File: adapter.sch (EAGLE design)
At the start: 10 parts

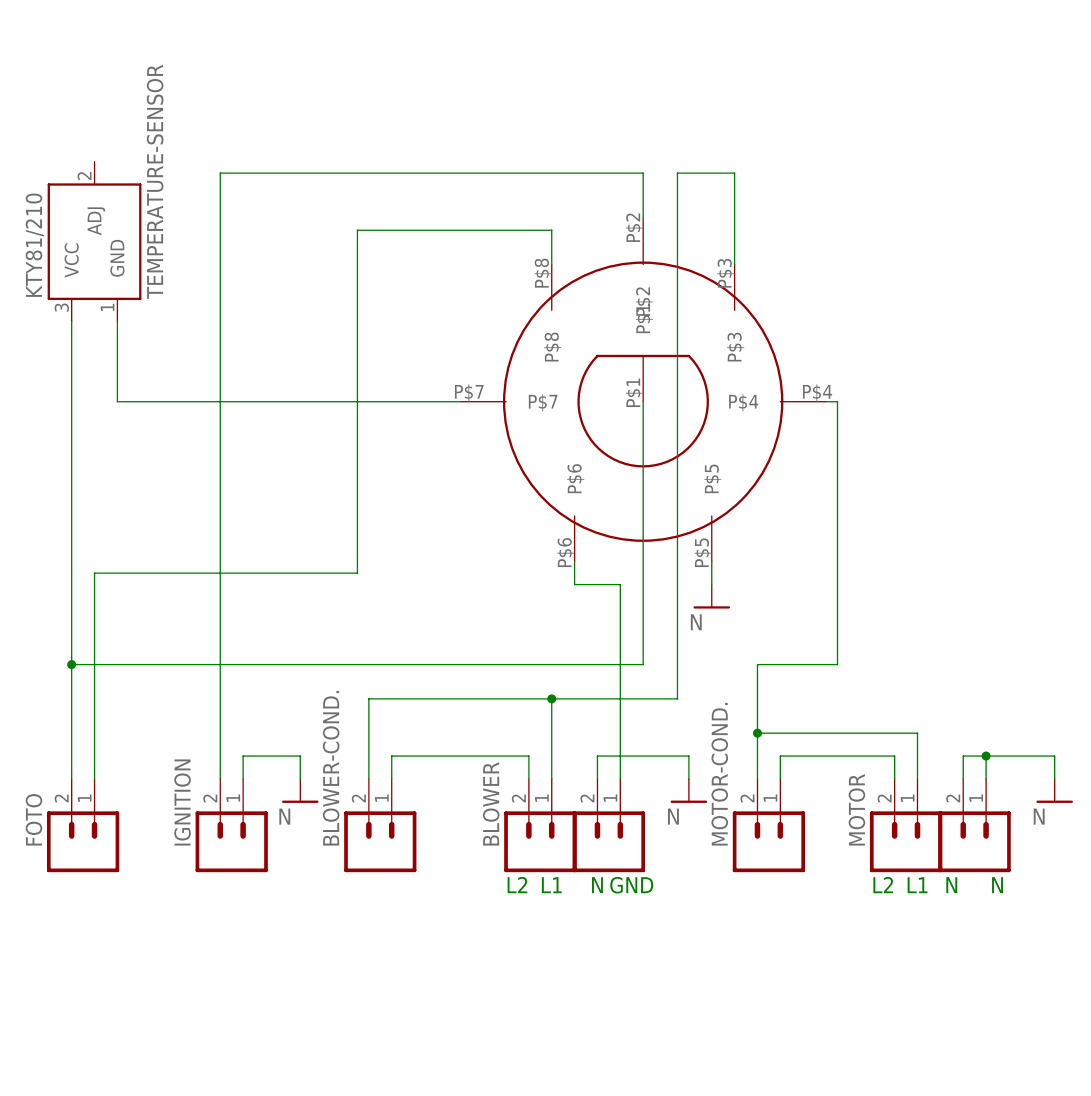
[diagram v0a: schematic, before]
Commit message: new version (v.1.4)
socket pin spacing changed from 5,02 mm to 5 mm

grouped photo and ignition connectors

added more silk info

wider pcb with space for capacitor hole mount
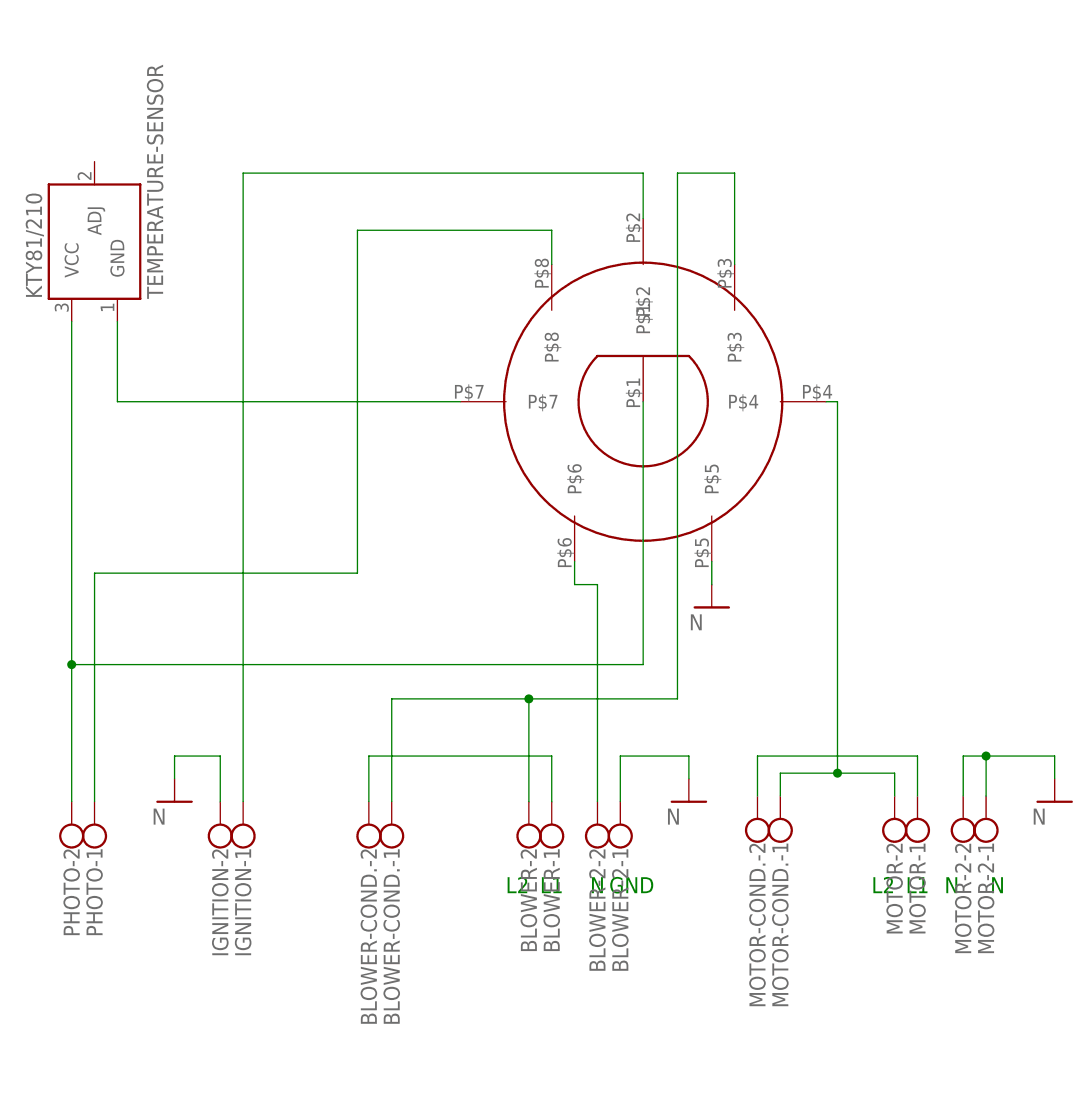
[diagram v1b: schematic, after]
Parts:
- removed BLOWER1, FOTO, MOTOR1: (no value), SparkFun (old):M02PTH3_5MM
- added BLOWER-2, MOTOR-2, PHOTO: (no value), con-wago-500:W237-102
- BLOWER, BLOWER-COND., IGNITION, MOTOR, MOTOR-COND.: device SparkFun (old):M02PTH3_5MM -> con-wago-500:W237-102
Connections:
- net GND: now also BLOWER-2-1.KL, IGNITION-2.KL, MOTOR-2-1.KL, MOTOR-2-2.KL; no longer BLOWER1.2, IGNITION.1, MOTOR1.1, MOTOR1.2
- net N$1: now also PHOTO-1.KL; no longer FOTO.1
- net N$10: now also MOTOR-2.KL, MOTOR-COND.-1.KL; no longer MOTOR-COND..2, MOTOR.1
- net N$2: now also IGNITION-1.KL; no longer IGNITION.2
- net N$3: now also PHOTO-2.KL; no longer FOTO.2
- net N$5: now also MOTOR-1.KL, MOTOR-COND.-2.KL; no longer MOTOR-COND..1, MOTOR.2
- net N$7: now also BLOWER-2.KL, BLOWER-COND.-1.KL; no longer BLOWER-COND..2, BLOWER.1
- net N$8: now also BLOWER-2-2.KL; no longer BLOWER1.1
- net N$9: now also BLOWER-1.KL, BLOWER-COND.-2.KL; no longer BLOWER-COND..1, BLOWER.2
